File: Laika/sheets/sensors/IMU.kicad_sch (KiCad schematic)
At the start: 3 parts, among them U7 LSM6DSRX

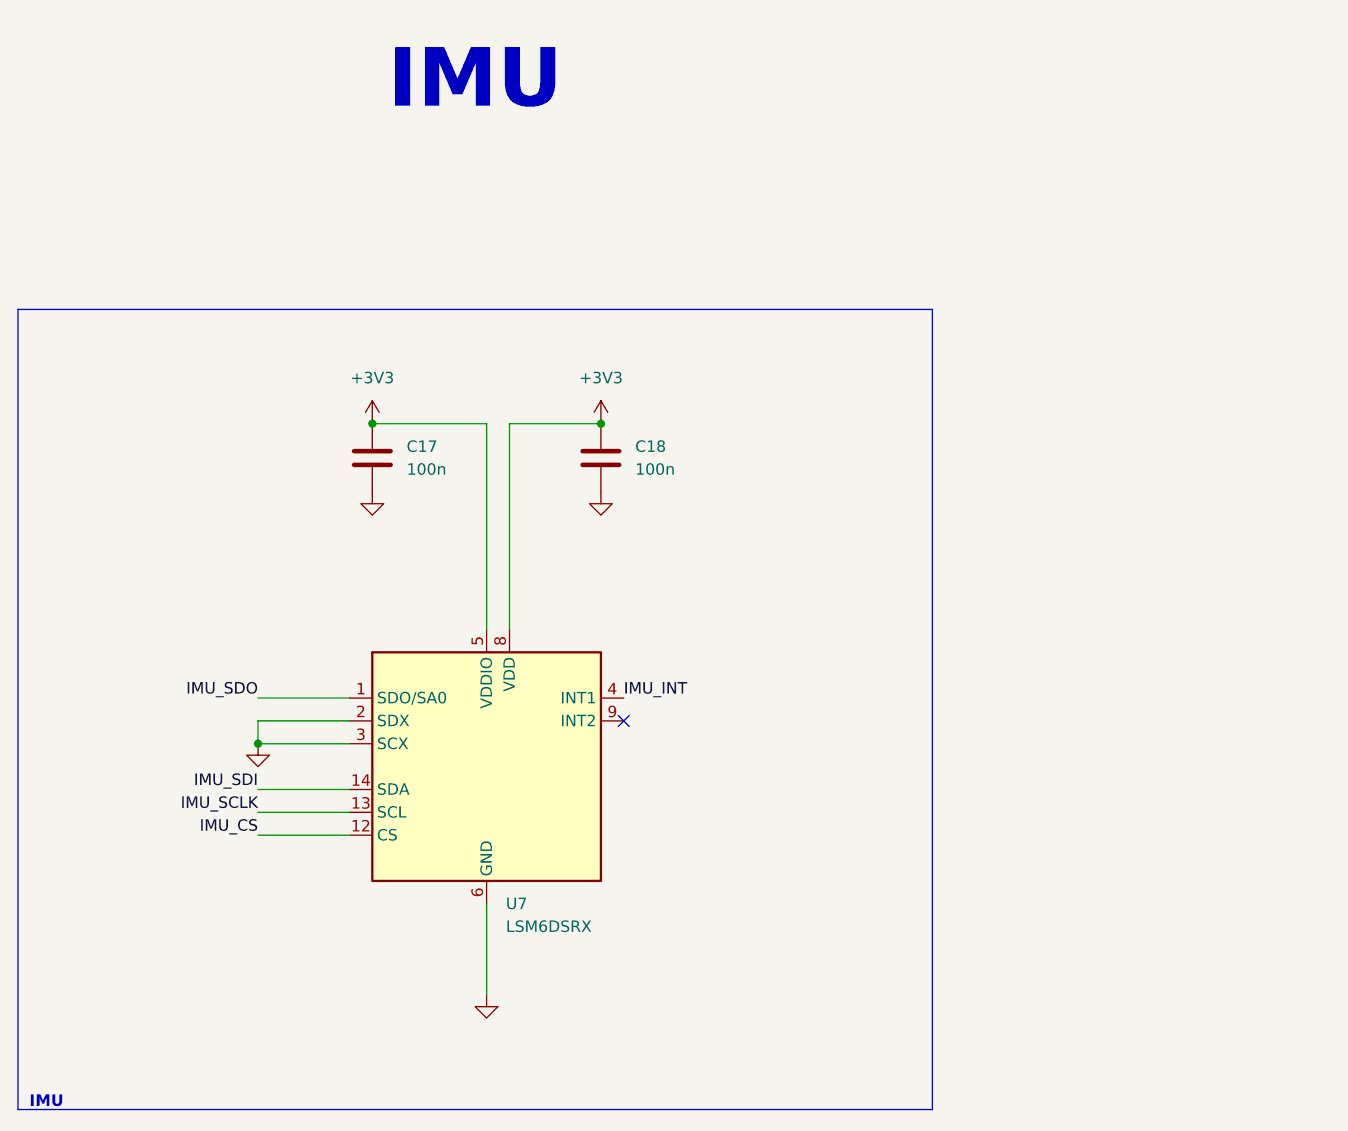
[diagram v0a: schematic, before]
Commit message: Connected sensors to SPI3
Connected Sensor Bus to SPI3. Rearranged GPS reset, pps, and buzzer pins
to other 3.3V logic pins. Connected SPI chip selects. Deleted interrupt
bus from sensors due to lack of 3.3V pins.
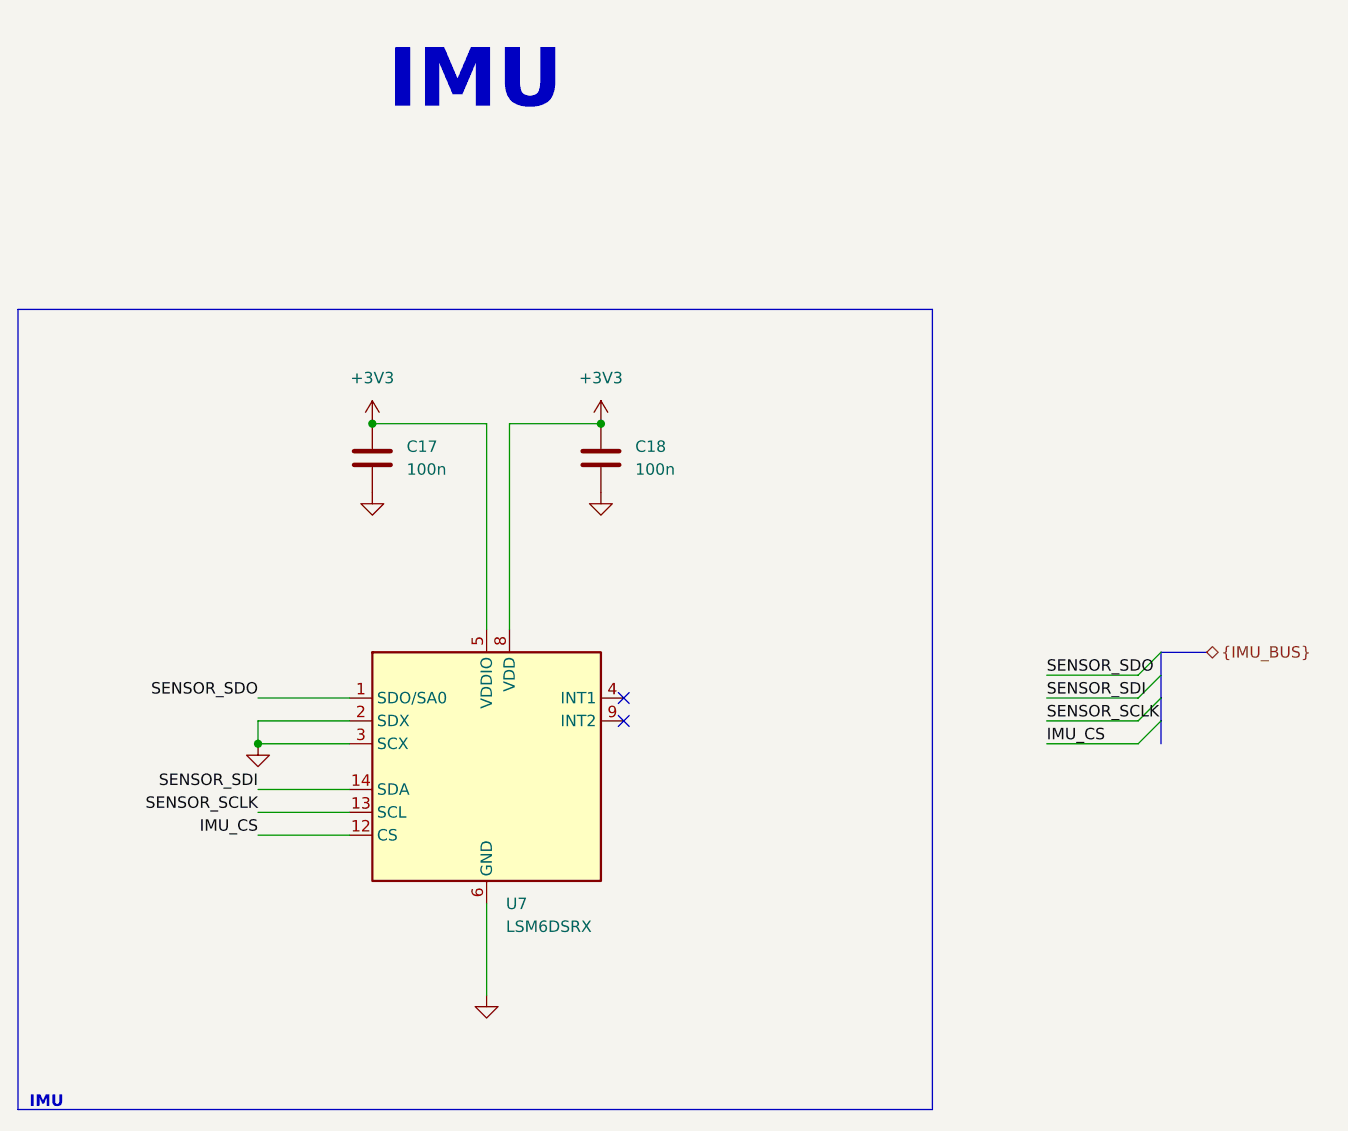
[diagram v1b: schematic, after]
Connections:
- net IMU_INT: no longer names the net of U7.4 (INT1)
- net IMU_SCLK renamed SENSOR_SCLK
- net IMU_SDI renamed SENSOR_SDI
- net IMU_SDO renamed SENSOR_SDO
- no-connect marks 1 -> 2
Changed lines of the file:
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@@
 		(at 156.21 96.52)
 	)
+	(no_connect
+		(at 156.21 93.98)
+	)
+	(bus_entry
+		(at 215.9 96.52)
+		(size -2.54 2.54)
+		(stroke
+			(width 0)
+			(type default)
+		)
+	)
+	(bus_entry
+		(at 215.9 91.44)
+		(size -2.54 2.54)
+		(stroke
+			(width 0)
+			(type default)
+		)
+	)
+	(bus_entry
+		(at 215.9 93.98)
+		(size -2.54 2.54)
+		(stroke
+			(width 0)
+			(type default)
+		)
+	)
+	(bus_entry
+		(at 215.9 88.9)
+		(size -2.54 2.54)
+		(stroke
+			(width 0)
+			(type default)
+		)
+	)
 	(wire
 		(pts
@@
 		)
 	)
+	(bus
+		(pts
+			(xy 220.98 88.9) (xy 215.9 88.9)
+		)
+		(stroke
+			(width 0)
+			(type default)
+		)
+	)
+	(bus
+		(pts
+			(xy 215.9 88.9) (xy 215.9 91.44)
+		)
+		(stroke
+			(width 0)
+			(type default)
+		)
+	)
 	(wire
 		(pts
@@
 		)
 	)
+	(bus
+		(pts
+			(xy 215.9 96.52) (xy 215.9 99.06)
+		)
+		(stroke
+			(width 0)
+			(type default)
+		)
+	)
 	(wire
 		(pts
@@
 	(wire
 		(pts
+			(xy 203.2 96.52) (xy 213.36 96.52)
+		)
+		(stroke
+			(width 0)
+			(type default)
+		)
+	)
+	(wire
+		(pts
+			(xy 203.2 93.98) (xy 213.36 93.98)
+		)
+		(stroke
+			(width 0)
+			(type default)
+		)
+	)
+	(wire
+		(pts
+			(xy 203.2 91.44) (xy 213.36 91.44)
+		)
+		(stroke
+			(width 0)
+			(type default)
+		)
+	)
+	(wire
+		(pts
 			(xy 115.57 96.52) (xy 115.57 99.06)
 		)
@@
 		)
 	)
-	(label "IMU_SCLK"
+	(wire
+		(pts
+			(xy 203.2 99.06) (xy 213.36 99.06)
+		)
+		(stroke
+			(width 0)
+			(type default)
+		)
+	)
+	(bus
+		(pts
+			(xy 215.9 91.44) (xy 215.9 93.98)
+		)
+		(stroke
+			(width 0)
+			(type default)
+		)
+	)
+	(bus
+		(pts
+			(xy 215.9 93.98) (xy 215.9 96.52)
+		)
+		(stroke
+			(width 0)
+			(type default)
+		)
+	)
+	(label "SENSOR_SCLK"
 		(at 115.57 106.68 180)
 		(effects
@@
 		)
 	)
-	(label "IMU_SDO"
+	(label "SENSOR_SDO"
 		(at 115.57 93.98 180)
 		(effects
@@
 		)
 	)
-	(label "IMU_SDI"
+	(label "IMU_CS"
+		(at 203.2 99.06 0)
+		(effects
+			(font
+				(size 1.27 1.27)
+			)
+			(justify left bottom)
+		)
+	)
+	(label "SENSOR_SDI"
 		(at 115.57 104.14 180)
 		(effects
@@
 		)
 	)
-	(label "IMU_INT"
-		(at 156.21 93.98 0)
+	(label "SENSOR_SDI"
+		(at 203.2 93.98 0)
+		(effects
+			(font
+				(size 1.27 1.27)
+			)
+			(justify left bottom)
+		)
+	)
+	(label "SENSOR_SDO"
+		(at 203.2 91.44 0)
 		(effects
 			(font
@@
 		)
 	)
+	(label "SENSOR_SCLK"
+		(at 203.2 96.52 0)
+		(effects
+			(font
+				(size 1.27 1.27)
+			)
+			(justify left bottom)
+		)
+	)
+	(hierarchical_label "{IMU_BUS}"
+		(shape bidirectional)
+		(at 220.98 88.9 0)
+		(effects
+			(font
+				(size 1.27 1.27)
+			)
+			(justify left)
+		)
+	)

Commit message: Populated BOM with part numbers and footprints
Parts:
- C17, C18: footprint (none) -> Capacitor_SMD:C_0402_1005Metric; JLC Part Type (none) -> Basic; Manafacturer (none) -> Samsung Electro-Mechanics; Part Number (none) -> CL05B104KO5NNNC
- U7: JLC Part Type (none) -> Extended; Manafacturer (none) -> STMicroelectronics; Part Number (none) -> LSM6DSRTR
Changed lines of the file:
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@@
+			)
+		)
+		(property "JLC Part Type" "Extended"
+			(at 140.97 101.6 0)
+			(effects
+				(font
+					(size 1.27 1.27)
+				)
+				(hide yes)
+			)
+		)
+		(property "Manafacturer" "STMicroelectronics"
+			(at 140.97 101.6 0)
+			(effects
+				(font
+					(size 1.27 1.27)
+				)
+				(hide yes)
+			)
+		)
+		(property "Part Number" "LSM6DSRTR"
+			(at 140.97 101.6 0)
+			(effects
+				(font
+					(size 1.27 1.27)
+				)
+				(hide yes)
 			)
 		)
@@
 			)
 		)
-		(property "Footprint" ""
+		(property "Footprint" "Capacitor_SMD:C_0402_1005Metric"
 			(at 129.2352 71.12 0)
 			(effects
@@
 			)
 		)
-		(property "Datasheet" "~"
+		(property "Datasheet" "https://www.samsungsem.com/resources/file/global/support/product_catalog/MLCC.pdf"
 			(at 128.27 67.31 0)
 			(effects
@@
 		)
 		(property "Description" "Unpolarized capacitor"
+			(at 128.27 67.31 0)
+			(effects
+				(font
+					(size 1.27 1.27)
+				)
+				(hide yes)
+			)
+		)
+		(property "JLC Part Type" "Basic"
+			(at 128.27 67.31 0)
+			(effects
+				(font
+					(size 1.27 1.27)
+				)
+				(hide yes)
+			)
+		)
+		(property "Manafacturer" "Samsung Electro-Mechanics"
+			(at 128.27 67.31 0)
+			(effects
+				(font
+					(size 1.27 1.27)
+				)
+				(hide yes)
+			)
+		)
+		(property "Part Number" "CL05B104KO5NNNC"
 			(at 128.27 67.31 0)
 			(effects
@@
 			)
 		)
-		(property "Footprint" ""
+		(property "Footprint" "Capacitor_SMD:C_0402_1005Metric"
 			(at 154.6352 71.12 0)
 			(effects
@@
 			)
 		)
-		(property "Datasheet" "~"
+		(property "Datasheet" "https://www.samsungsem.com/resources/file/global/support/product_catalog/MLCC.pdf"
 			(at 153.67 67.31 0)
 			(effects
@@
 			(at 153.67 67.31 0)
 			(effects
+				(font
+					(size 1.27 1.27)
+				)
+				(hide yes)
+			)
+		)
+		(property "JLC Part Type" "Basic"
+			(at 153.67 67.31 0)
+			(effects
+				(font
+					(size 1.27 1.27)
+				)
+				(hide yes)
+			)
+		)
+		(property "Manafacturer" "Samsung Electro-Mechanics"
+			(at 153.67 67.31 0)
+			(effects
+				(font
+					(size 1.27 1.27)
+				)
+				(hide yes)
+			)
+		)
+		(property "Part Number" "CL05B104KO5NNNC"
+			(at 153.67 67.31 0)
+			(effects
